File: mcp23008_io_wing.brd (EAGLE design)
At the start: 50.8 x 22.9 mm, 16 parts

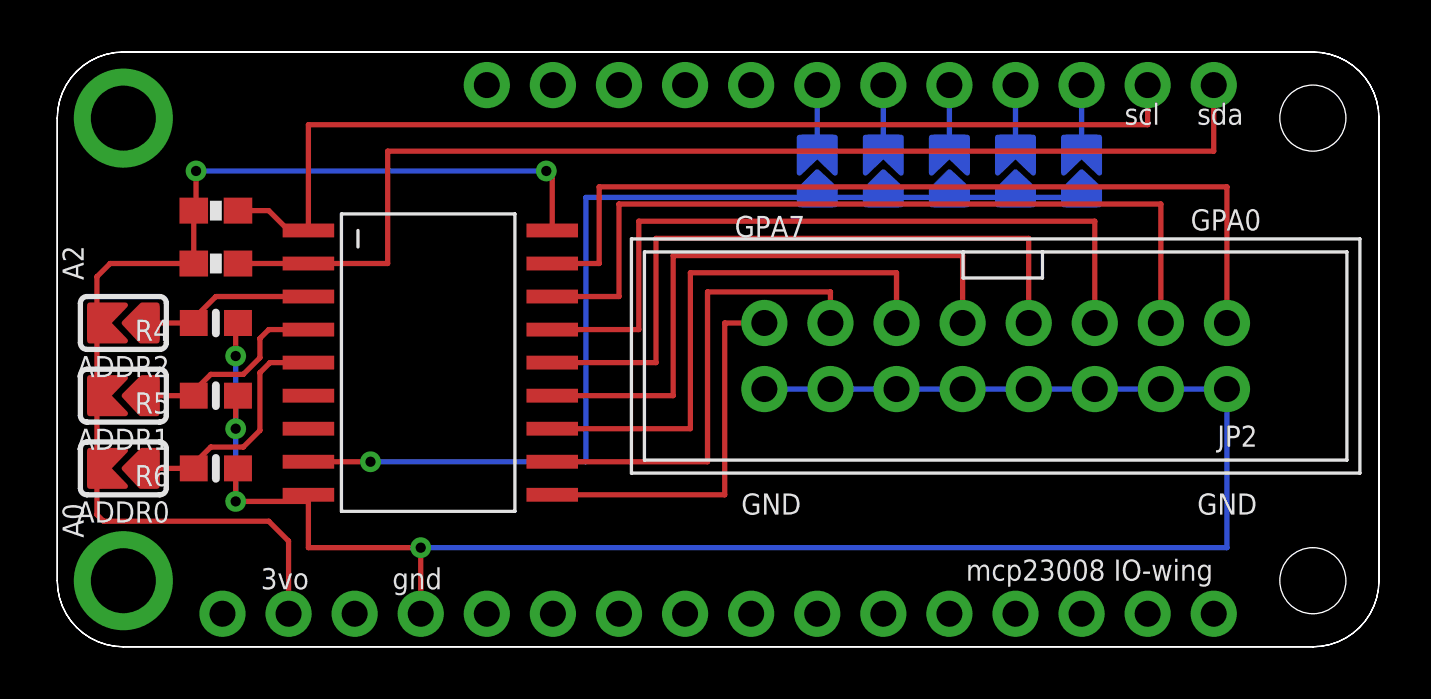
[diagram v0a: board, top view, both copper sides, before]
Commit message: updated board and pcb images
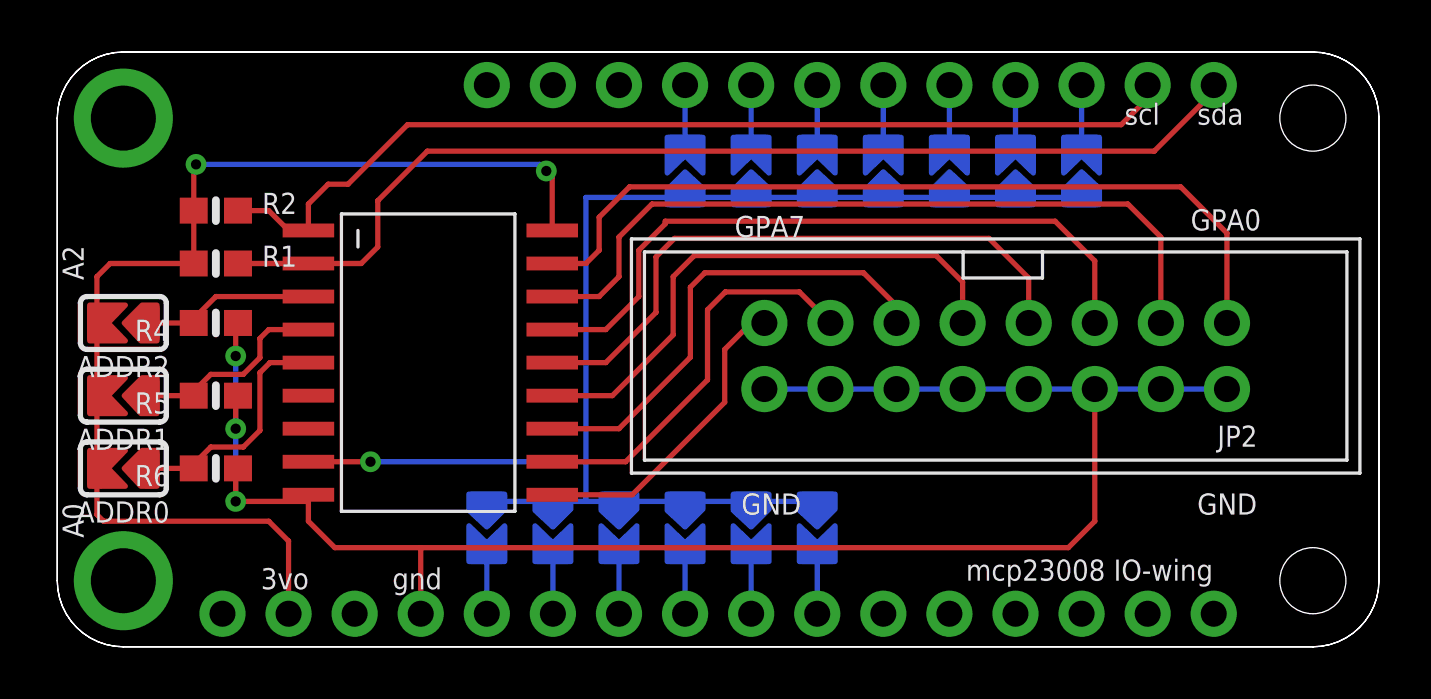
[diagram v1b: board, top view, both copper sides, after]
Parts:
- removed R7, R8: 10K, rickk2:0603-RES
- added INT10, INT11, INT12, INT13, INT6, INT7, INT8, INT9: (no value), microbuilder:SOLDERJUMPER_ARROW_NOPASTE
- added R1, R2: 10K, microbuilder:0603-NO
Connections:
- new net N$10: INT10.2, MS1.7
- new net N$11: INT11.2, MS1.8
- new net N$12: INT12.2, MS1.9
- new net N$13: INT13.2, MS1.10
- new net N$4: INT6.2, MS1.24
- new net N$5: INT7.2, MS1.25
- new net N$6: INT8.2, MS1.5
- new net N$9: INT9.2, MS1.6
- net 3V: now also R1.1, R2.1; no longer R7.2, R8.2
- net INT: now also INT10.1, INT11.1, INT12.1, INT13.1, INT6.1, INT7.1, INT8.1, INT9.1
- net SCL: now also R2.2; no longer R8.1
- net SDA: now also R1.2; no longer R7.1
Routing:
- net INT: track 39.9 -> 54.1 mm
- net GND: track 76.4 -> 69.8 mm, vias 4 -> 3
- net GPA6: track 18.4 -> 15.5 mm
- net SDA: track 44.4 -> 41.5 mm
- net GPA7: track 14.8 -> 12.1 mm
- net GPA5: track 21.2 -> 18.5 mm
- net GPA4: track 23.7 -> 21.3 mm
- net GPA3: track 26.3 -> 23.9 mm
- net SCL: track 40.9 -> 38.5 mm
- net N$5: track 0.00 -> 2.29 mm
- net N$4: track 0.00 -> 2.29 mm
- net N$9: track 0.00 -> 2.29 mm
- net N$6: track 0.00 -> 2.29 mm
- net N$13: track 0.00 -> 2.29 mm
- net N$12: track 0.00 -> 2.29 mm
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
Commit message: pcb v2
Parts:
- removed R1, R2: 10K, microbuilder:0603-NO
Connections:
- removed net VCC: U$2.6
- net 3V: now also U$2.6; no longer R1.1, R2.1
- net SCL: no longer R2.2
- net SDA: no longer R1.2
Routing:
- net 3V: track 43.5 -> 57.3 mm, vias 2 -> 3
- net SDA: track 41.5 -> 38.8 mm
- net SCL: track 38.5 -> 36.2 mm
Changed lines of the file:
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@@
 <text x="26.289" y="5.08" size="0.8128" layer="21" font="vector" ratio="12">GND</text>
 <text x="43.815" y="5.08" size="0.8128" layer="21" font="vector" ratio="12">GND</text>
-<text x="26.035" y="15.748" size="0.8128" layer="21" font="vector" ratio="12">GPA7</text>
-<text x="43.561" y="16.002" size="0.8128" layer="21" font="vector" ratio="12">GPA0</text>
+<text x="26.035" y="15.748" size="0.8128" layer="21" font="vector" ratio="12">GPA0</text>
+<text x="43.561" y="16.002" size="0.8128" layer="21" font="vector" ratio="12">GPA7</text>
 <text x="1.016" y="14.097" size="0.8128" layer="21" font="vector" ratio="12" rot="R90">A2</text>
 <text x="1.016" y="4.191" size="0.8128" layer="21" font="vector" ratio="12" rot="R90">A0</text>
@@
 <attribute name="VALUE" x="30.861" y="6.223" size="0.4064" layer="28" ratio="10" rot="MR270"/>
 </element>
-<element name="R1" library="microbuilder" package="0603-NO" value="10K" x="6.096" y="14.732" smashed="yes">
-<attribute name="NAME" x="7.874" y="14.605" size="0.8128" layer="25" font="vector" ratio="18"/>
-<attribute name="VALUE" x="7.874" y="13.97" size="0.4064" layer="27" font="vector" ratio="10"/>
-</element>
-<element name="R2" library="microbuilder" package="0603-NO" value="10K" x="6.096" y="16.764" smashed="yes">
-<attribute name="NAME" x="7.874" y="16.637" size="0.8128" layer="25" font="vector" ratio="18"/>
-<attribute name="VALUE" x="7.874" y="16.002" size="0.4064" layer="27" font="vector" ratio="10"/>
-</element>
 </elements>
 <signals>
@@
 <wire x1="18.796" y1="18.288" x2="19.0246" y2="18.0594" width="0.2032" layer="1"/>
 <wire x1="19.0246" y1="18.0594" x2="19.0246" y2="16.002" width="0.2032" layer="1"/>
-<wire x1="18.542" y1="18.542" x2="5.334" y2="18.542" width="0.2032" layer="16"/>
+<wire x1="18.542" y1="18.542" x2="15.494" y2="18.542" width="0.2032" layer="16"/>
+<wire x1="15.494" y1="18.542" x2="5.334" y2="18.542" width="0.2032" layer="16"/>
 <wire x1="18.542" y1="18.542" x2="18.796" y2="18.288" width="0.2032" layer="16"/>
 <via x="5.334" y="18.542" extent="1-16" drill="0.3937"/>
@@
 <wire x1="1.524" y1="14.224" x2="1.524" y2="12.446" width="0.2032" layer="1"/>
 <wire x1="8.128" y1="4.826" x2="8.89" y2="4.064" width="0.2032" layer="1"/>
-<contactref element="R1" pad="1"/>
-<contactref element="R2" pad="1"/>
-<wire x1="5.246" y1="14.732" x2="2.032" y2="14.732" width="0.2032" layer="1"/>
-<wire x1="5.246" y1="14.732" x2="5.246" y2="16.764" width="0.2032" layer="1"/>
-<wire x1="5.246" y1="16.764" x2="5.246" y2="18.454" width="0.2032" layer="1"/>
 <wire x1="5.246" y1="18.454" x2="5.334" y2="18.542" width="0.2032" layer="1"/>
+<wire x1="5.334" y1="18.542" x2="5.334" y2="16.002" width="0.2032" layer="1"/>
+<wire x1="5.334" y1="16.002" x2="4.064" y2="14.732" width="0.2032" layer="1"/>
+<wire x1="4.064" y1="14.732" x2="2.032" y2="14.732" width="0.2032" layer="1"/>
+<wire x1="15.494" y1="18.542" x2="15.494" y2="10.668" width="0.2032" layer="16"/>
+<wire x1="15.494" y1="10.668" x2="14.478" y2="9.652" width="0.2032" layer="16"/>
+<wire x1="14.478" y1="9.652" x2="11.938" y2="9.652" width="0.2032" layer="16"/>
+<contactref element="U$2" pad="6"/>
+<wire x1="11.938" y1="9.652" x2="11.62685" y2="9.652" width="0.2032" layer="16"/>
+<via x="11.938" y="9.652" extent="1-16" drill="0.3937"/>
+<wire x1="9.652" y1="9.652" x2="11.938" y2="9.652" width="0.2032" layer="1"/>
 </signal>
 <signal name="SCL">
@@
 <wire x1="40.894" y1="20.066" x2="13.462" y2="20.066" width="0.2032" layer="1"/>
 <wire x1="9.652" y1="17.018" x2="9.652" y2="16.002" width="0.2032" layer="1"/>
-<wire x1="8.128" y1="16.764" x2="8.89" y2="16.002" width="0.2032" layer="1"/>
 <wire x1="8.89" y1="16.002" x2="9.652" y2="16.002" width="0.2032" layer="1"/>
-<contactref element="R2" pad="2"/>
-<wire x1="6.946" y1="16.764" x2="8.128" y2="16.764" width="0.2032" layer="1"/>
 <wire x1="40.894" y1="20.066" x2="41.91" y2="21.082" width="0.2032" layer="1"/>
 <wire x1="41.91" y1="21.082" x2="41.91" y2="21.59" width="0.2032" layer="1"/>
@@
 <wire x1="42.164" y1="19.05" x2="14.224" y2="19.05" width="0.2032" layer="1"/>
 <wire x1="9.652" y1="14.732" x2="11.684" y2="14.732" width="0.2032" layer="1"/>
-<contactref element="R1" pad="2"/>
-<wire x1="6.946" y1="14.732" x2="9.652" y2="14.732" width="0.2032" layer="1"/>
 <wire x1="42.164" y1="19.05" x2="44.45" y2="21.336" width="0.2032" layer="1"/>
 <wire x1="44.45" y1="21.336" x2="44.45" y2="21.59" width="0.2032" layer="1"/>
@@
 <wire x1="36.83" y1="19.304" x2="36.83" y2="21.59" width="0.2032" layer="16"/>
 </signal>
-<signal name="VCC">
-<contactref element="U$2" pad="6"/>
-</signal>
 <signal name="N$4">
